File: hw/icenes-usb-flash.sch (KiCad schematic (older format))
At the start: 29 parts, among them U4 iCE40HX8K-CT256, U5 93LC56C-I_SN, U6 FT2232H, U7 AT25SF041-SSHD, X1 DSC1001DI2-012.0000

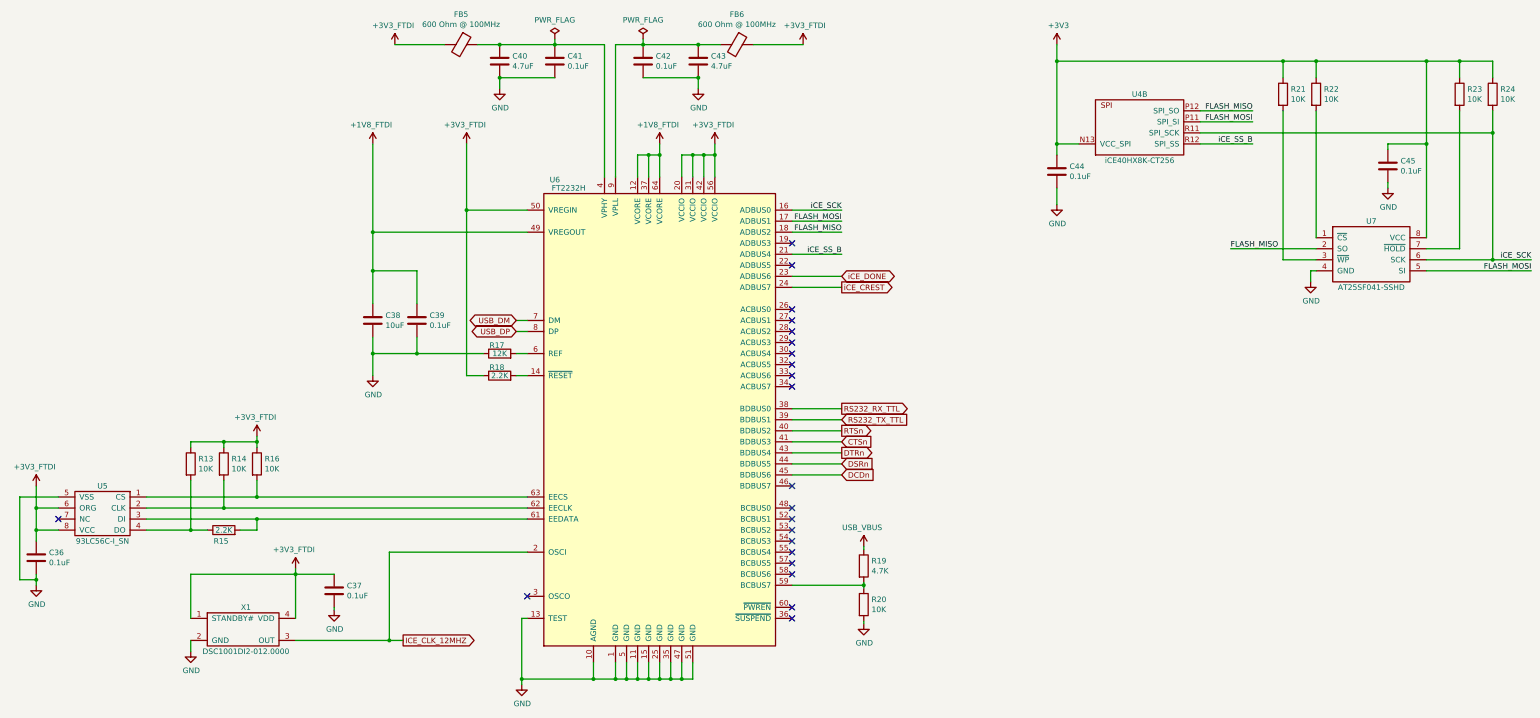
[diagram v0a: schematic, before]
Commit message: Added voltage range in Vin lable (+5V to +10V).
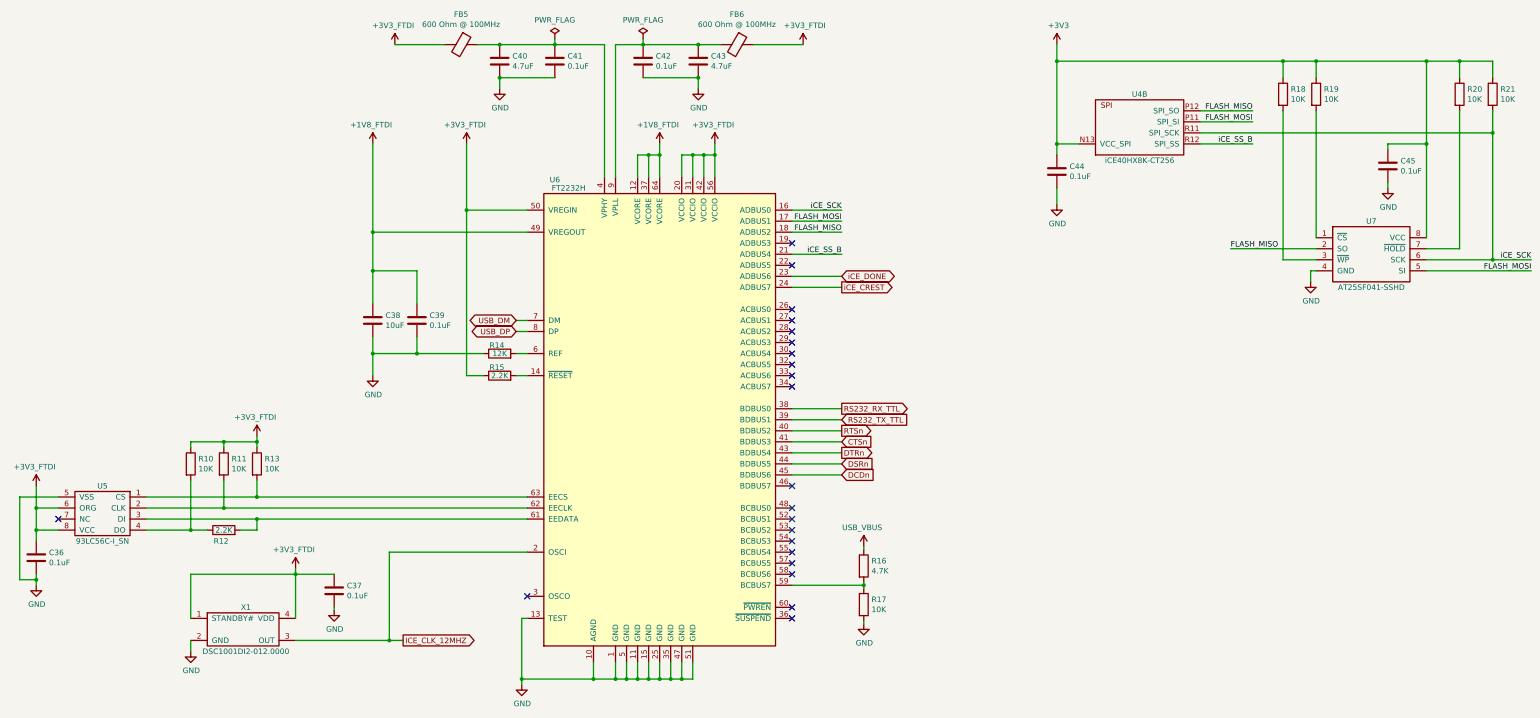
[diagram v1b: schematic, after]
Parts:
- renumbered R13 to R10, R14 to R11, R15 to R12, R16 to R13, R17 to R14, R18 to R15, R19 to R16, R20 to R17, R21 to R18, R22 to R19, R23 to R20, R24 to R21
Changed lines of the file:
@@
 	5650 7500 5650 7550
 $Comp
-L icenes-library:R2.2K R18
+L icenes-library:R2.2K R15
 U 1 1 5D0ACC8C
 P 5450 4750
-F 0 "R18" H 5425 4825 50  0000 C CNN
+F 0 "R15" H 5425 4825 50  0000 C CNN
 F 1 "R2.2K" H 5450 4650 50  0001 C CNN
 F 2 "Resistor_SMD:R_0603_1608Metric_Pad1.05x0.95mm_HandSolder" V 5450 4750 50  0001 C CNN
@@
 $EndComp
 $Comp
-L icenes-library:R10K R16
+L icenes-library:R10K R13
 U 1 1 5D1569F2
 P 3250 5550
-F 0 "R16" V 3204 5620 50  0000 L CNN
+F 0 "R13" V 3204 5620 50  0000 L CNN
 F 1 "R10K" H 3250 5450 50  0001 C CNN
 F 2 "Resistor_SMD:R_0603_1608Metric_Pad1.05x0.95mm_HandSolder" V 3250 5550 50  0001 C CNN
@@
 $EndComp
 $Comp
-L icenes-library:R10K R14
+L icenes-library:R10K R11
 U 1 1 5D157EB6
 P 2950 5550
-F 0 "R14" V 2904 5620 50  0000 L CNN
+F 0 "R11" V 2904 5620 50  0000 L CNN
 F 1 "R10K" H 2950 5450 50  0001 C CNN
 F 2 "Resistor_SMD:R_0603_1608Metric_Pad1.05x0.95mm_HandSolder" V 2950 5550 50  0001 C CNN
@@
 $EndComp
 $Comp
-L icenes-library:R10K R13
+L icenes-library:R10K R10
 U 1 1 5D159230
 P 2650 5550
-F 0 "R13" V 2604 5620 50  0000 L CNN
+F 0 "R10" V 2604 5620 50  0000 L CNN
 F 1 "R10K" H 2650 5450 50  0001 C CNN
 F 2 "Resistor_SMD:R_0603_1608Metric_Pad1.05x0.95mm_HandSolder" V 2650 5550 50  0001 C CNN
@@
 Connection ~ 2950 5350
 $Comp
-L icenes-library:R2.2K R15
+L icenes-library:R2.2K R12
 U 1 1 5D165DEC
 P 2950 6150
-F 0 "R15" H 2925 6050 50  0000 C CNN
+F 0 "R12" H 2925 6050 50  0000 C CNN
 F 1 "R2.2K" H 2950 6050 50  0001 C CNN
 F 2 "Resistor_SMD:R_0603_1608Metric_Pad1.05x0.95mm_HandSolder" V 2950 6150 50  0001 C CNN
@@
 	10500 2650 10500 2750
 $Comp
-L icenes-library:R10K R24
+L icenes-library:R10K R21
 U 1 1 5D4A0315
 P 14450 2200
-F 0 "R24" V 14404 2270 50  0000 L CNN
+F 0 "R21" V 14404 2270 50  0000 L CNN
 F 1 "R10K" H 14450 2100 50  0001 C CNN
 F 2 "Resistor_SMD:R_0603_1608Metric_Pad1.05x0.95mm_HandSolder" V 14450 2200 50  0001 C CNN
@@
 	12800 3800 12800 3900
 $Comp
-L icenes-library:R10K R22
+L icenes-library:R10K R19
 U 1 1 5D1B0361
 P 12850 2200
-F 0 "R22" V 12804 2270 50  0000 L CNN
+F 0 "R19" V 12804 2270 50  0000 L CNN
 F 1 "R10K" H 12850 2100 50  0001 C CNN
 F 2 "Resistor_SMD:R_0603_1608Metric_Pad1.05x0.95mm_HandSolder" V 12850 2200 50  0001 C CNN
@@
 $EndComp
 $Comp
-L icenes-library:R10K R21
+L icenes-library:R10K R18
 U 1 1 5D1B1707
 P 12550 2200
-F 0 "R21" V 12504 2270 50  0000 L CNN
+F 0 "R18" V 12504 2270 50  0000 L CNN
 F 1 "R10K" H 12550 2100 50  0001 C CNN
 F 2 "Resistor_SMD:R_0603_1608Metric_Pad1.05x0.95mm_HandSolder" V 12550 2200 50  0001 C CNN
@@
 	13850 2650 13850 3500
 $Comp
-L icenes-library:R10K R23
+L icenes-library:R10K R20
 U 1 1 5D1AE89D
 P 14150 2200
-F 0 "R23" V 14104 2270 50  0000 L CNN
+F 0 "R20" V 14104 2270 50  0000 L CNN
 F 1 "R10K" H 14150 2100 50  0001 C CNN
 F 2 "Resistor_SMD:R_0603_1608Metric_Pad1.05x0.95mm_HandSolder" V 14150 2200 50  0001 C CNN
@@
 DCDn
 $Comp
-L icenes-library:R12K R17
+L icenes-library:R12K R14
 U 1 1 5D987F0F
 P 5450 4550
-F 0 "R17" H 5425 4625 50  0000 C CNN
+F 0 "R14" H 5425 4625 50  0000 C CNN
 F 1 "R12K" H 5450 4450 50  0001 C CNN
 F 2 "Resistor_SMD:R_0603_1608Metric_Pad1.05x0.95mm_HandSolder" H 5450 4650 50  0001 C CNN
@@
 $EndComp
 $Comp
-L icenes-library:R10K R20
+L icenes-library:R10K R17
 U 1 1 5D987FF0
 P 8750 6825
-F 0 "R20" V 8704 6895 50  0000 L CNN
+F 0 "R17" V 8704 6895 50  0000 L CNN
 F 1 "R10K" H 8750 6725 50  0001 C CNN
 F 2 "Resistor_SMD:R_0603_1608Metric_Pad1.05x0.95mm_HandSolder" V 8750 6825 50  0001 C CNN
@@
 $EndComp
 $Comp
-L icenes-library:R4.7K R19
+L icenes-library:R4.7K R16
 U 1 1 5D99454A
 P 8750 6475
-F 0 "R19" V 8704 6545 50  0000 L CNN
+F 0 "R16" V 8704 6545 50  0000 L CNN
 F 1 "R4.7K" H 8750 6375 50  0001 C CNN
 F 2 "Resistor_SMD:R_0603_1608Metric_Pad1.05x0.95mm_HandSolder" V 8750 6475 50  0001 C CNN

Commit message: Added missing footprint for the new inductor. Added 3d models to the barrel jack and oscillators.
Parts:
- X1: footprint Crystal:Crystal_SMD_2520-4Pin_2.5x2.0mm -> icenes-library:MEMS_Microship_Ocillator_SMD_CDFN-4_2.5x2.0mm
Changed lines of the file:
@@
 F 0 "X1" H 3150 6850 50  0000 C CNN
 F 1 "DSC1001DI2-012.0000" H 3150 6450 50  0000 C CNN
-F 2 "Crystal:Crystal_SMD_2520-4Pin_2.5x2.0mm" H 3250 6900 50  0001 C CNN
+F 2 "icenes-library:MEMS_Microship_Ocillator_SMD_CDFN-4_2.5x2.0mm" H 3250 6900 50  0001 C CNN
 F 3 "https://ww1.microchip.com/downloads/en/DeviceDoc/20005529B.pdf" H 3250 6900 50  0001 C CNN
 F 4 "Microchip" H 3150 6850 50  0001 C CNN "Manufacturer"

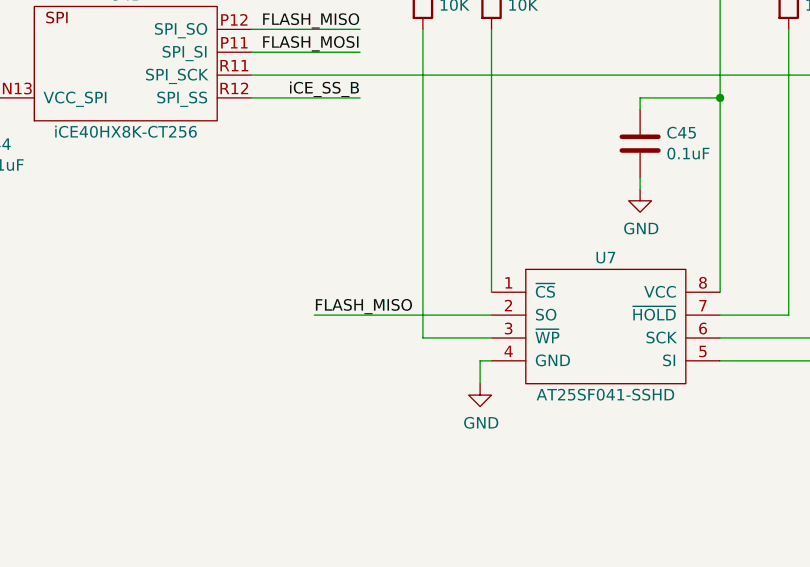
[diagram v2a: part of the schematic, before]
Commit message: Connected the chip select pin of the SPI flash to FT2232H and to the FPGA.
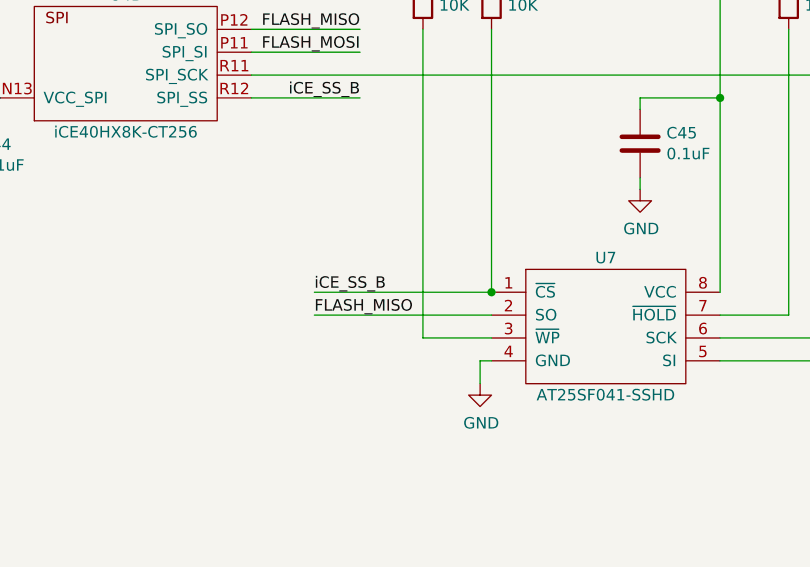
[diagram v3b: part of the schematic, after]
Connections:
- net iCE_SS_B: now also R19.2, U7.1 (~CS)
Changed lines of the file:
@@
 	10500 1900 12550 1900
-Wire Wire Line
-	12850 3500 12850 2350
 Wire Wire Line
 	12850 2050 12850 1900
@@
 Text Label 8550 3650 2    50   ~ 0
 iCE_SS_B
-Text Label 12275 2650 2    50   ~ 0
-iCE_SS_B
 Text Label 12275 2450 2    50   ~ 0
 FLASH_MOSI
@@
 Wire Wire Line
 	13850 3800 14800 3800
-Wire Wire Line
-	11800 2650 12275 2650
 Text GLabel 8550 5050 2    50   Output ~ 0
 RS232_RX_TTL
@@
 Wire Wire Line
 	5950 1700 5950 1750
+Text Label 12075 3500 0    50   ~ 0
+iCE_SS_B
+Wire Wire Line
+	12075 3500 12850 3500
+Connection ~ 12850 3500
+Wire Wire Line
+	12850 3500 12850 2350
+Wire Wire Line
+	11800 2650 12275 2650
+Text Label 12275 2650 2    50   ~ 0
+iCE_SS_B
 $EndSCHEMATC
